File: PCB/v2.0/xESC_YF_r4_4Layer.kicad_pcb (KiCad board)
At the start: 2 copper layers, 49.5 x 29 mm, 50 parts, among them J1 Conn_01x09_Male, J10 OM-MB W => MC BRK, J2 Conn_01x03_Pin, J3 Conn_01x05_Male, J4 Conn_01x05_Male, J6 OM-MB U <= MC SA, J7 Conn_01x06_Male, J8 Conn_01x06_Pin, J9 OM-MB V => MC +24V, Q1 2N7002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

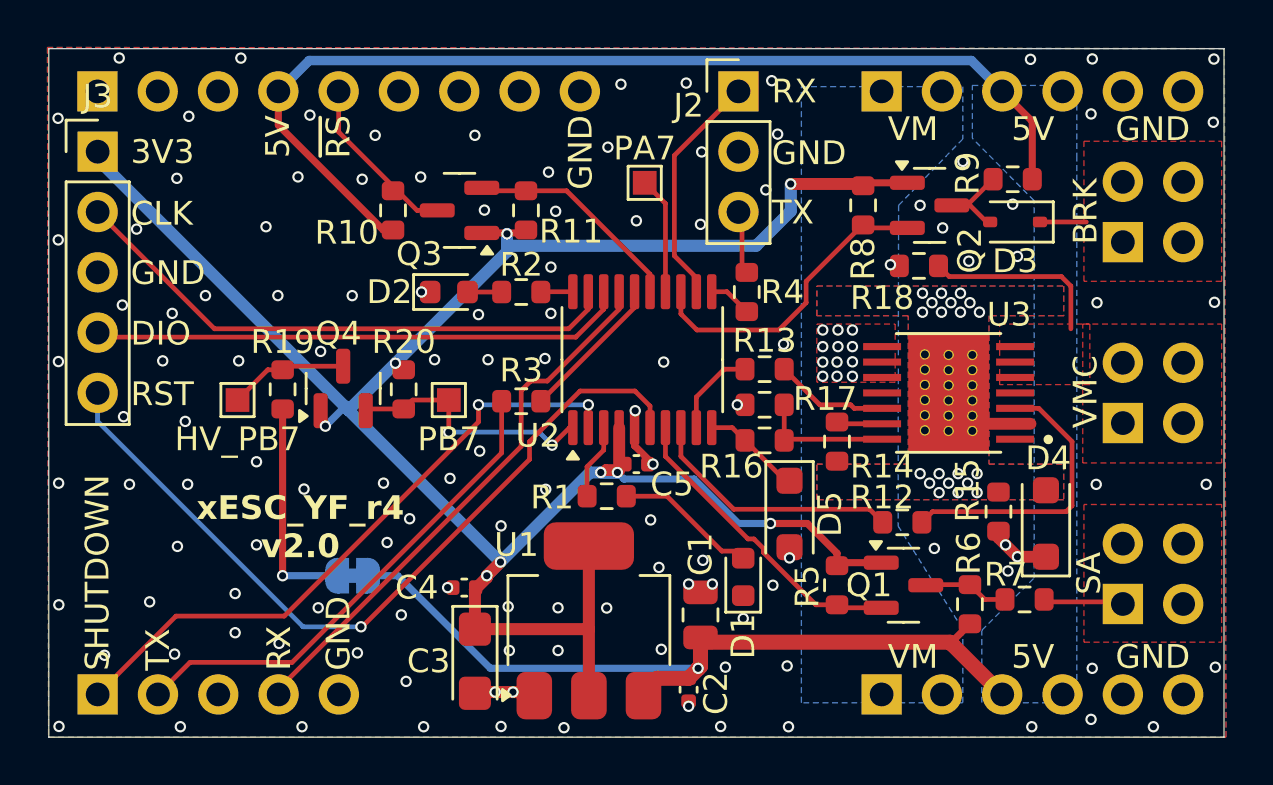
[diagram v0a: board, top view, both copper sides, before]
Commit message: Add HW v2.0
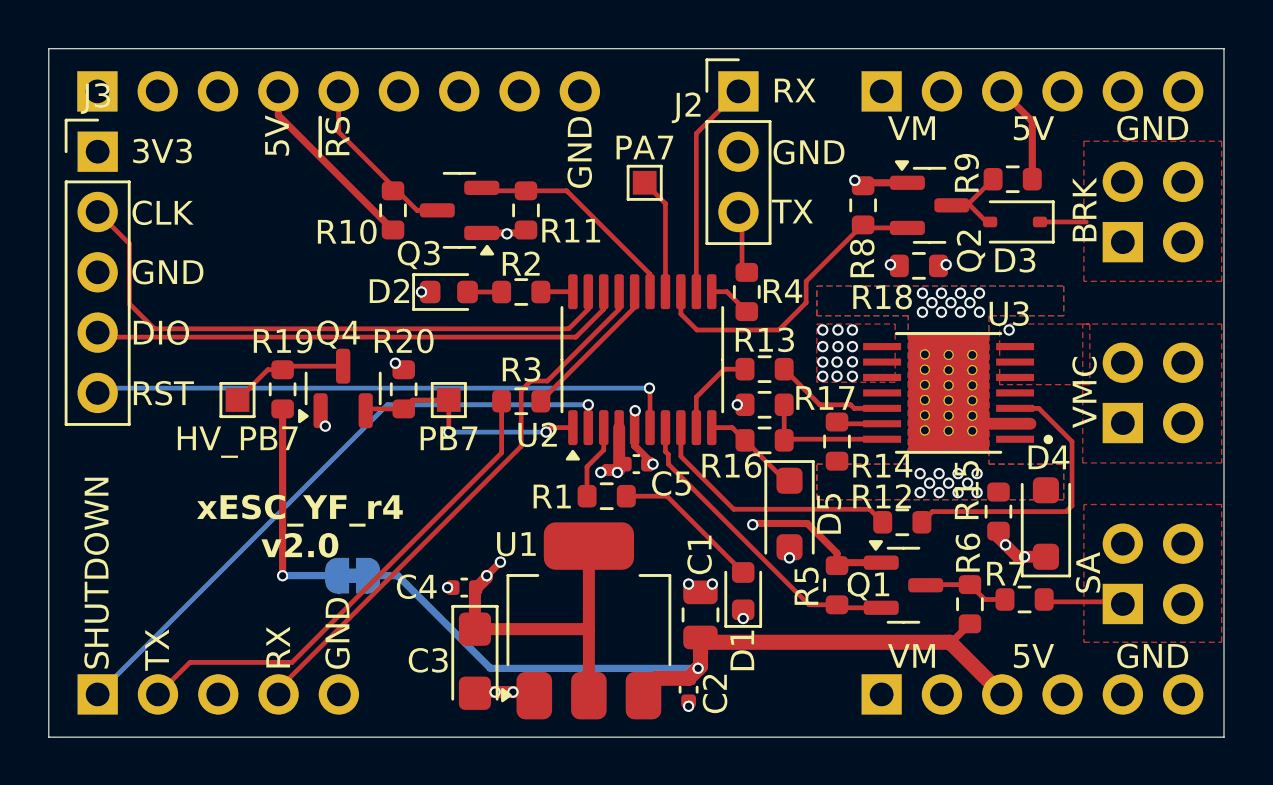
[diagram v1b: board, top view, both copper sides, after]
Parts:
- moved D1 0.60 mm to (258.2, 126.8)
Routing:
- net /NRST: track 33.9 -> 24.7 mm
- net Net-(J9-Pin_1): track 7.73 -> 4.55 mm, vias 0 -> 2
- net /SWCLK: track 23.8 -> 25.3 mm
- net +3V3: track 95.5 -> 94.7 mm
- net /SHUTDOWN: track 27.1 -> 26.7 mm, vias 2 -> 1
- net GND: vias 126 -> 14
- net Net-(D4-A): vias 20 -> 22
- added copper zone on In2.Cu, net +5V
- added copper zone on In1.Cu, net GND
- added copper zone on In2.Cu, net VM
- removed copper zone on B.Cu, net +5V
- removed copper zone on B.Cu, net GND
- removed copper zone on F.Cu, net GND
- removed copper zone on B.Cu, net VM
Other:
- copper layers 2 -> 4
